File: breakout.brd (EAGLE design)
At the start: 100 x 80 mm, 26 parts

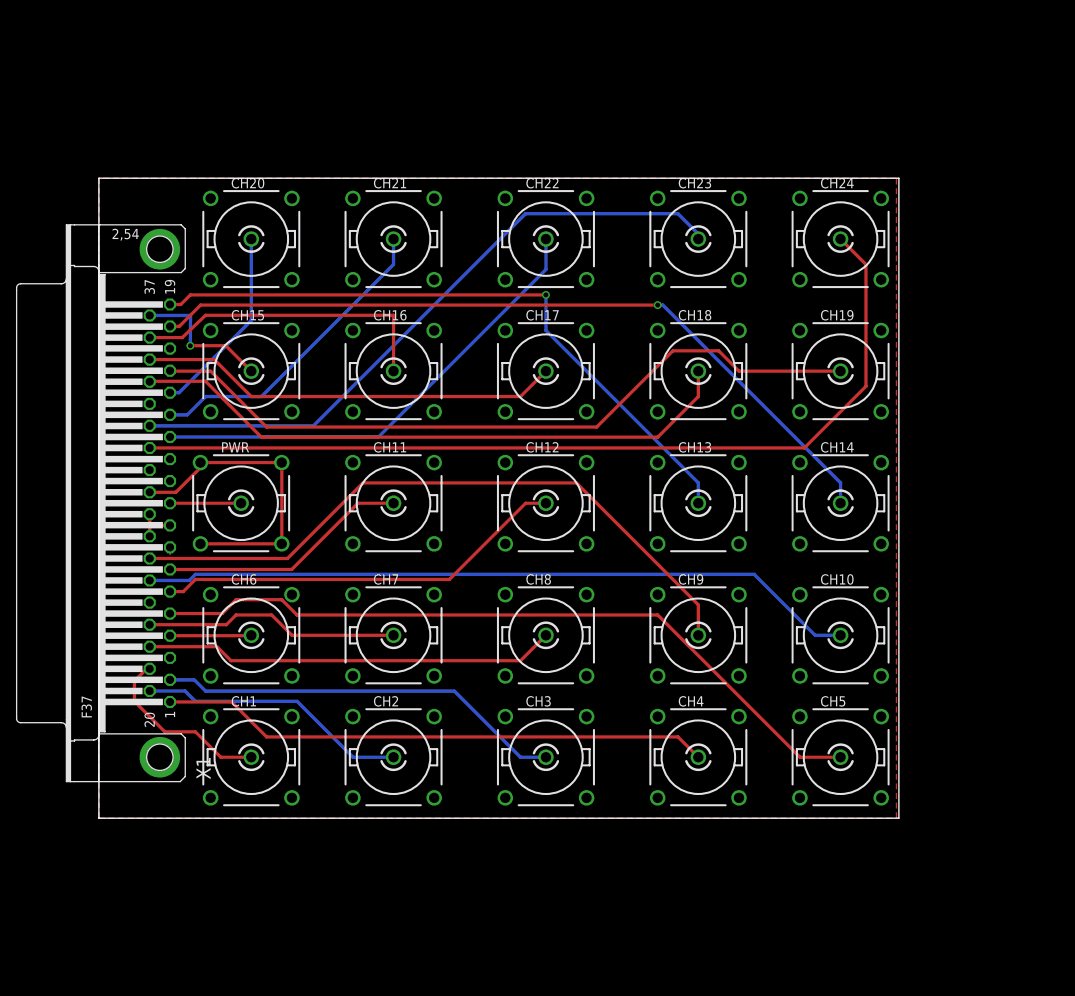
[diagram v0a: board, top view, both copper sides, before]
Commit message: minor labeling and component placement updates. most significant is correcting part position on powerboard so 22uF bypass cap actually connects to ground.
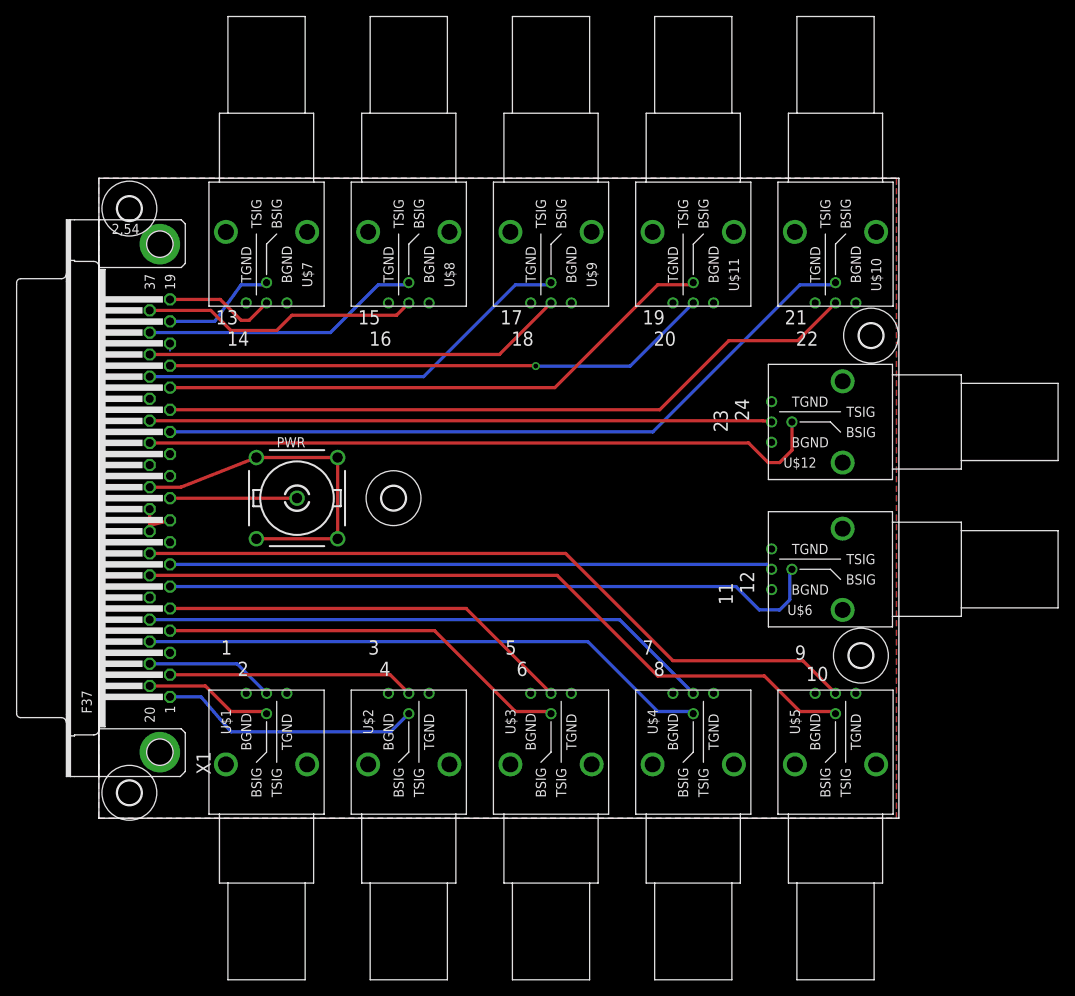
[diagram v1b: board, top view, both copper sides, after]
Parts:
- removed CH1, CH10, CH11, CH12, CH13, CH14, CH15, CH16, CH17, CH18, CH19, CH2, CH20, CH21, CH22, CH23, CH24, CH3, CH4, CH5, CH6, CH7, CH8, CH9: R141426, con-coax:R141426
- added PAD1, PAD2, PAD3, PAD4, PAD5: MOUNT-HOLE3.0, holes:3,0
- added U$1, U$10, U$11, U$12, U$2, U$3, U$4, U$5, U$6, U$7, U$8, U$9: 031-6575, 031-6575:031-6575
- moved PWR 7.01 mm to (24.8, 40.0)
- moved X1 0.64 mm to (7.62, 40.0)
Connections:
- net CH1: now also U$1.1; no longer CH1.1
- net CH10: now also U$5.3; no longer CH10.1
- net CH11: now also U$6.1; no longer CH11.1
- net CH12: now also U$6.3; no longer CH12.1
- net CH13: now also U$7.1; no longer CH13.1
- net CH14: now also U$7.3; no longer CH14.1
- net CH15: now also U$8.1; no longer CH15.1
- net CH16: now also U$8.3; no longer CH16.1
- net CH17: now also U$9.1; no longer CH17.1
- net CH18: now also U$9.3; no longer CH18.1
- net CH19: now also U$11.1; no longer CH19.1
- net CH2: now also U$1.3; no longer CH2.1
- net CH20: now also U$11.3; no longer CH20.1
- net CH21: now also U$10.1; no longer CH21.1
- net CH22: now also U$10.3; no longer CH22.1
- net CH23: now also U$12.1; no longer CH23.1
- net CH24: now also U$12.3; no longer CH24.1
- net CH3: now also U$2.1; no longer CH3.1
- net CH4: now also U$2.3; no longer CH4.1
- net CH5: now also U$3.1; no longer CH5.1
- net CH6: now also U$3.3; no longer CH6.1
- net CH7: now also U$4.1; no longer CH7.1
- net CH8: now also U$4.3; no longer CH8.1
- net CH9: now also U$5.1; no longer CH9.1
- net VREF: now also U$1.2, U$1.4, U$10.2, U$10.4, U$11.2, U$11.4, U$12.2, U$12.4, U$2.2, U$2.4, U$3.2, U$3.4, U$4.2, U$4.4, U$5.2, U$5.4, U$6.2, U$6.4, U$7.2, U$7.4, U$8.2, U$8.4, U$9.2, U$9.4; no longer CH1.2, CH1.3, CH1.4, CH1.5, CH10.2, CH10.3, CH10.4, CH10.5, CH11.2, CH11.3, CH11.4, CH11.5, CH12.2, CH12.3, CH12.4, CH12.5, CH13.2, CH13.3, CH13.4, CH13.5, CH14.2, CH14.3, CH14.4, CH14.5, CH15.2, CH15.3, CH15.4, CH15.5, CH16.2, CH16.3, CH16.4, CH16.5, CH17.2, CH17.3, CH17.4, CH17.5, CH18.2, CH18.3, CH18.4, CH18.5, CH19.2, CH19.3, CH19.4, CH19.5, CH2.2, CH2.3, CH2.4, CH2.5, CH20.2, CH20.3, CH20.4, CH20.5, CH21.2, CH21.3, CH21.4, CH21.5, CH22.2, CH22.3, CH22.4, CH22.5, CH23.2, CH23.3, CH23.4, CH23.5, CH24.2, CH24.3, CH24.4, CH24.5, CH3.2, CH3.3, CH3.4, CH3.5, CH4.2, CH4.3, CH4.4, CH4.5, CH5.2, CH5.3, CH5.4, CH5.5, CH6.2, CH6.3, CH6.4, CH6.5, CH7.2, CH7.3, CH7.4, CH7.5, CH8.2, CH8.3, CH8.4, CH8.5, CH9.2, CH9.3, CH9.4, CH9.5
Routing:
- net CH14: track 96.7 -> 14.5 mm, vias 1 -> 0
- net CH13: track 81.4 -> 14.0 mm, vias 1 -> 0
- net CH21: track 38.9 -> 88.7 mm
- net CH20: track 24.1 -> 70.8 mm
- net CH11: track 31.4 -> 75.5 mm
- net CH6: track 10.2 -> 51.9 mm
- net CH5: track 92.7 -> 52.0 mm
- net CH7: track 32.0 -> 71.8 mm
- net CH4: track 68.9 -> 32.8 mm
- net CH12: track 51.6 -> 83.1 mm
- net CH22: track 59.5 -> 90.9 mm
- net CH24: track 112.5 -> 85.5 mm
- net CH19: track 91.7 -> 68.7 mm, vias 0 -> 1
- net CH18: track 76.8 -> 55.0 mm
- net CH3: track 51.0 -> 30.8 mm
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- added copper zone on layer 16, net GND
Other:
- board text added: "1 2"
- board text added: "11 12"
- board text added: "13 14"
- board text added: "15 16"
- board text added: "17 18"
- board text added: "19 20"
- board text added: "21 22"
- board text added: "23 24"
- board text added: "3 4"
- board text added: "5 6"
- board text added: "7 8"
- board text added: "9 10"
- board text added: "Rev3 Feb 2017"
- board text removed: "Rev1 Sept 2016"
